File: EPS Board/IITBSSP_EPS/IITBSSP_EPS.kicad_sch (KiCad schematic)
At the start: 7 parts, among them J1 USB_B_Micro, J3 Screw_Terminal_01x02

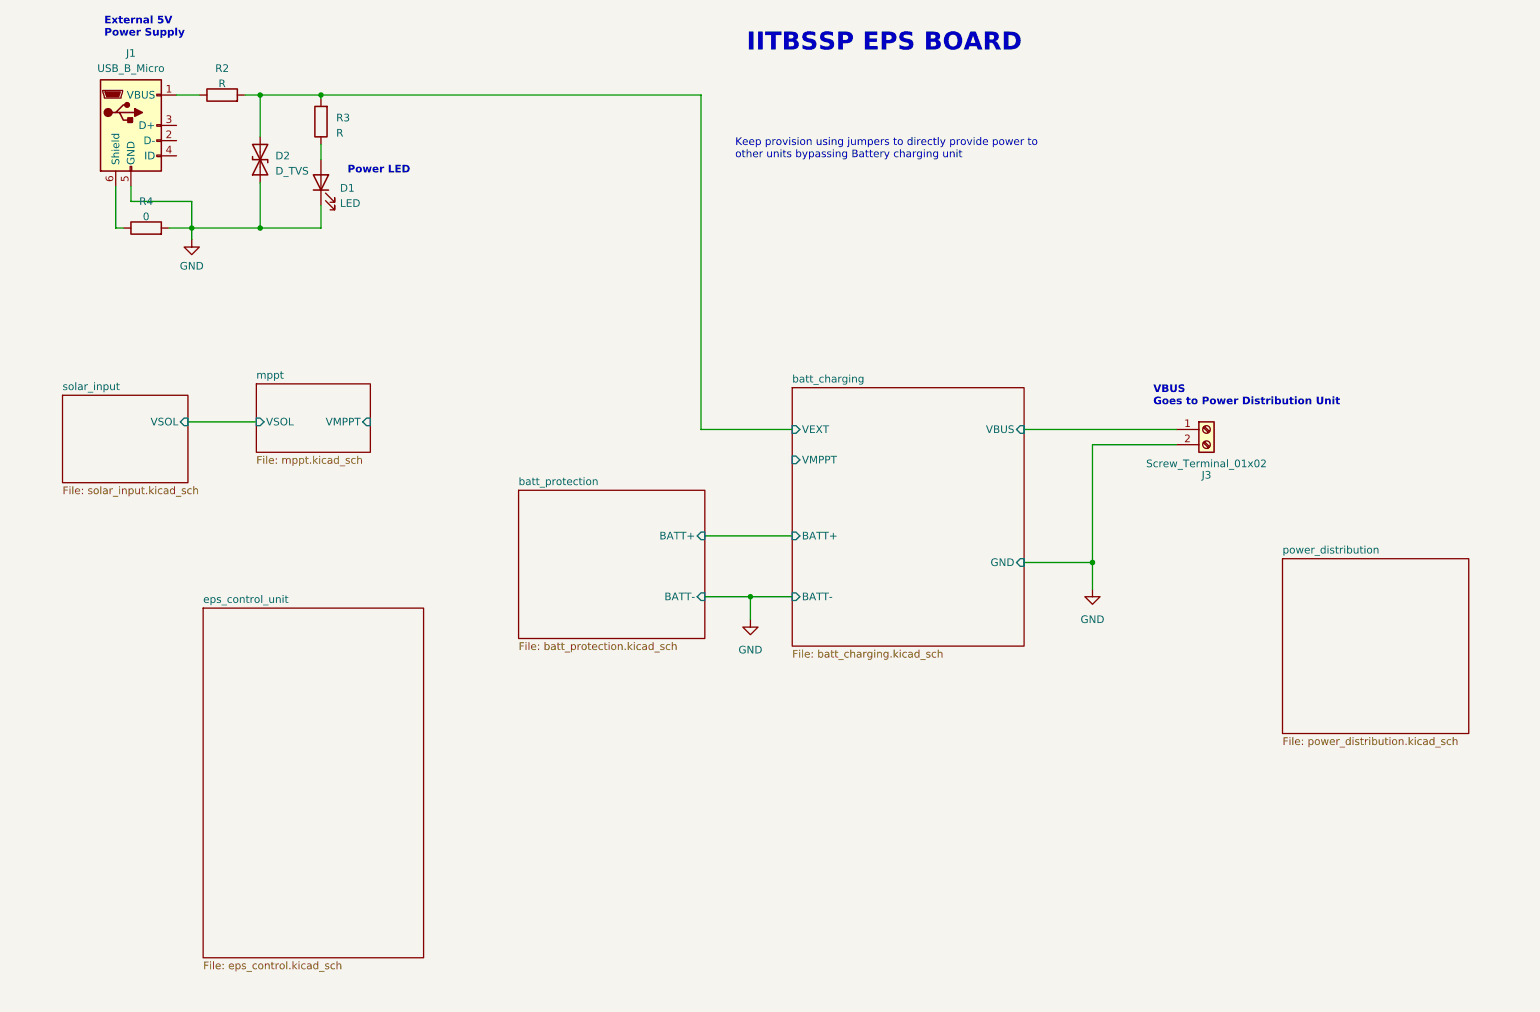
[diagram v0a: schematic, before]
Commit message: EPS Control Unit Dev and Final Schematic designed
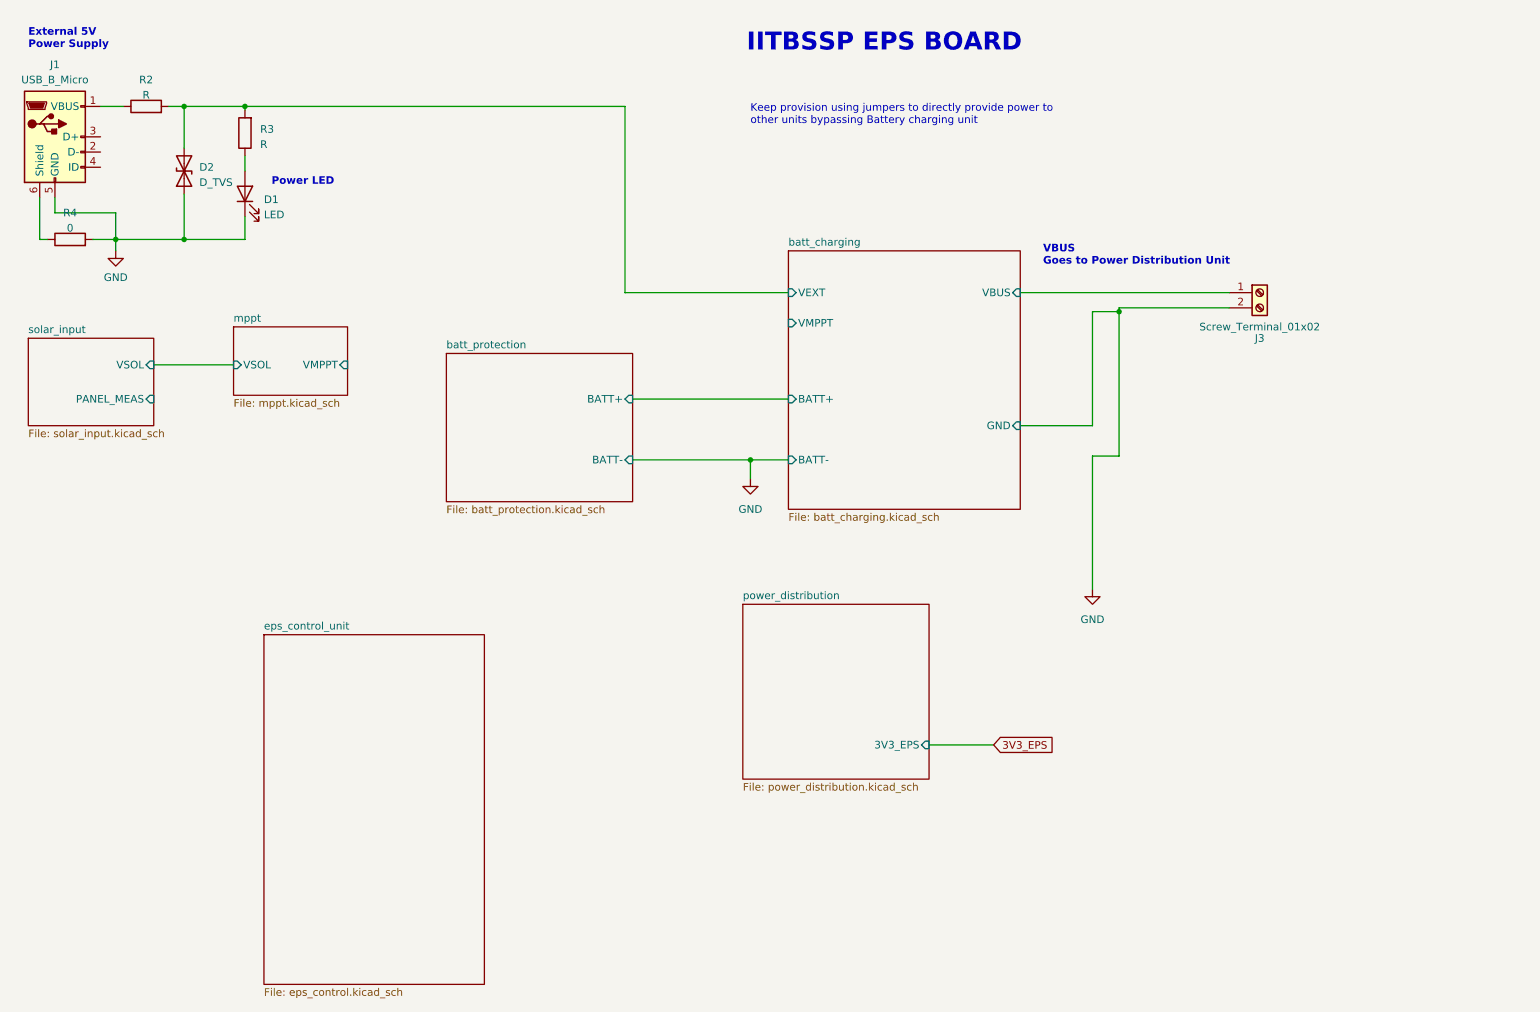
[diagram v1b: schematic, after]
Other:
- sheet power_distribution ports: added 3V3_EPS; removed none
- sheet solar_input ports: added PANEL_MEAS; removed none
- moved on the sheet: D1, D2, J1, J3, R2, R3, R4
